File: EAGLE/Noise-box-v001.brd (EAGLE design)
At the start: 160 x 100 mm, 2 parts, among them J1 AVR_SPI_PROG_3X22X3_LOCK, U1 ATMEGA328P_TQFP

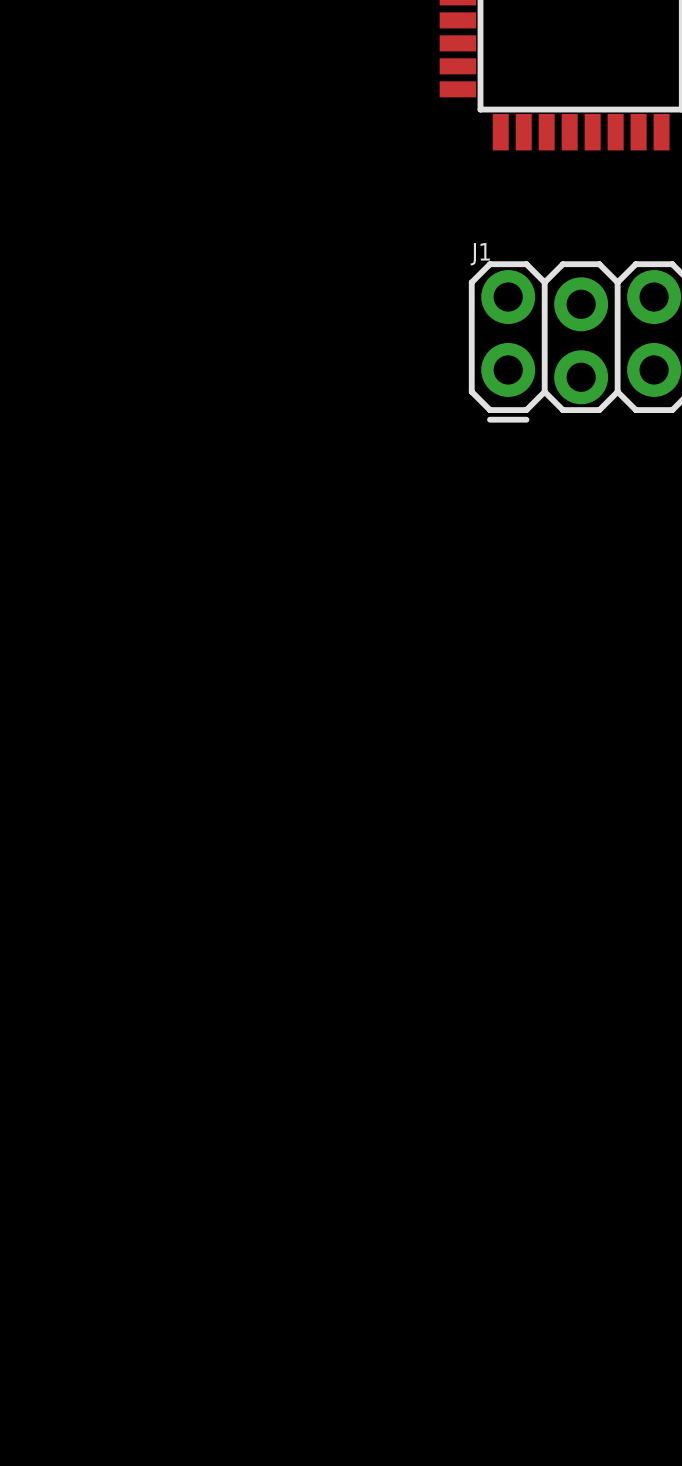
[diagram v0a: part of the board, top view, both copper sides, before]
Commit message: Sch update - power
Added voltage regulators and supporting components.
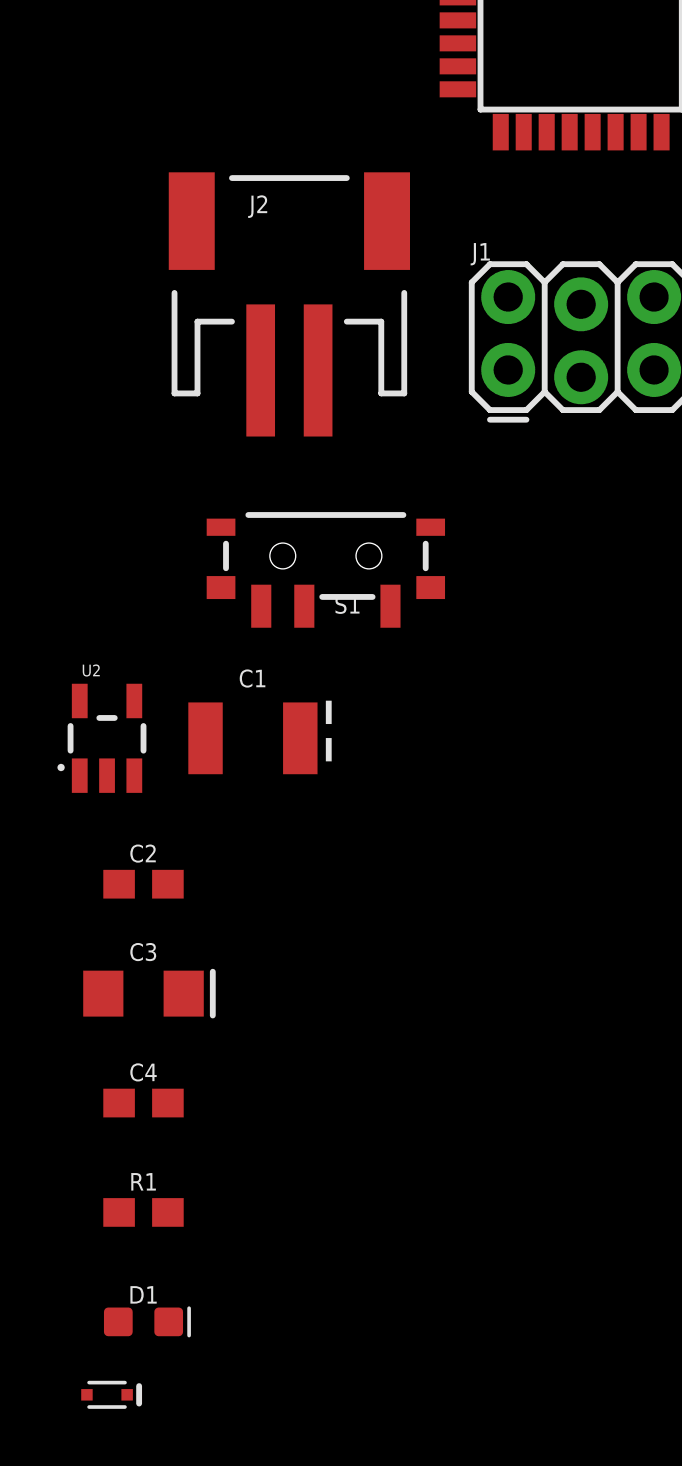
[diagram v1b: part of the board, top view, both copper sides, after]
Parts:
- added C1: 47uF, SparkFun-Capacitors:EIA3528
- added C2: 470pF, SparkFun-Capacitors:0603
- added C3: 10uF, SparkFun-Capacitors:EIA3216
- added C4: 0.1uF, SparkFun-Capacitors:0603
- added D1: RED, SparkFun-LED:LED-0603
- added D2: 120mA/40V/370mV, SparkFun-DiscreteSemi:SOD-523
- added J2: BATT, SparkFun-Connectors:JST-2-SMD
- added R1: 330, SparkFun-Resistors:0603
- added S1: (no value), SparkFun-Switches:SWITCH_SPST_SMD_A
- added U2: MIC5219 3.3V, SparkFun-IC-Power:SOT23-5
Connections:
- new net N$2: C2.1, U2.4
- new net N$3: D1.A, R1.2
- new net V+: C1.A, D2.C, S1.1, U2.1, U2.3
- new net VBATT: J2.1, S1.2
- net +3V3: now also C3.+, C4.1, D2.A, R1.1, U2.5
- net GND: now also C1.C, C2.2, C3.-, C4.2, D1.C, J2.2, U2.2
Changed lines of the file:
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@@
 </element>
 <element name="J1" library="SparkFun-Connectors" package="2X3_LOCK" value="AVR_SPI_PROG_3X22X3_LOCK" x="-7.62" y="-5.08"/>
+<element name="J2" library="SparkFun-Connectors" package="JST-2-SMD" value="BATT" x="-15.24" y="-1.27">
+<attribute name="PROD_ID" value="CONN-11443" x="-15.24" y="-1.27" size="1.778" layer="27" display="off"/>
+</element>
+<element name="S1" library="SparkFun-Switches" package="SWITCH_SPST_SMD_A" value="" x="-13.97" y="-11.43">
+<attribute name="SF_SKU" value="COM-10860" x="-13.97" y="-11.43" size="1.778" layer="27" display="off"/>
+<attribute name="PROD_ID" value="SWCH-10651" x="-13.97" y="-11.43" size="1.778" layer="27" display="off"/>
+</element>
+<element name="C1" library="SparkFun-Capacitors" package="EIA3528" value="47uF" x="-16.51" y="-17.78">
+<attribute name="PROD_ID" value="CAP-08310" x="-16.51" y="-17.78" size="1.778" layer="27" display="off"/>
+</element>
+<element name="U2" library="SparkFun-IC-Power" package="SOT23-5" value="MIC5219 3.3V" x="-21.59" y="-17.78">
+<attribute name="PROD_ID" value="VREG-09872" x="-21.59" y="-17.78" size="1.778" layer="27" display="off"/>
+</element>
+<element name="C2" library="SparkFun-Capacitors" package="0603" value="470pF" x="-20.32" y="-22.86">
+<attribute name="PROD_ID" value="CAP-07884" x="-20.32" y="-22.86" size="1.778" layer="27" display="off"/>
+</element>
+<element name="C3" library="SparkFun-Capacitors" package="EIA3216" value="10uF" x="-20.32" y="-26.67">
+<attribute name="PROD_ID" value="CAP-00811" x="-20.32" y="-26.67" size="1.778" layer="27" display="off"/>
+</element>
+<element name="C4" library="SparkFun-Capacitors" package="0603" value="0.1uF" x="-20.32" y="-30.48">
+<attribute name="PROD_ID" value="CAP-08604" x="-20.32" y="-30.48" size="1.778" layer="27" display="off"/>
+</element>
+<element name="R1" library="SparkFun-Resistors" package="0603" value="330" x="-20.32" y="-34.29">
+<attribute name="PROD_ID" value="RES-00818" x="-20.32" y="-34.29" size="1.778" layer="27" display="off"/>
+</element>
+<element name="D1" library="SparkFun-LED" package="LED-0603" value="RED" x="-20.32" y="-38.1">
+<attribute name="PROD_ID" value="DIO-00819" x="-20.32" y="-38.1" size="1.778" layer="27" display="off"/>
+</element>
+<element name="D2" library="SparkFun-DiscreteSemi" package="SOD-523" value="120mA/40V/370mV" x="-21.59" y="-40.64">
+<attribute name="PROD_ID" value="DIO-11018" x="-21.59" y="-40.64" size="1.778" layer="27" display="off"/>
+</element>
 </elements>
 <signals>
@@
 <contactref element="U1" pad="18"/>
 <contactref element="J1" pad="2"/>
+<contactref element="U2" pad="5"/>
+<contactref element="R1" pad="1"/>
+<contactref element="C3" pad="+"/>
+<contactref element="C4" pad="1"/>
+<contactref element="D2" pad="A"/>
+<wire x1="-21.17" y1="-34.29" x2="-22.29" y2="-40.64" width="0" layer="19" extent="1-1"/>
+<wire x1="-21.17" y1="-30.48" x2="-21.17" y2="-34.29" width="0" layer="19" extent="1-1"/>
+<wire x1="-18.92" y1="-26.67" x2="-21.17" y2="-30.48" width="0" layer="19" extent="1-1"/>
+<wire x1="-22.54" y1="-16.4799" x2="-18.92" y2="-26.67" width="0" layer="19" extent="1-1"/>
+<wire x1="-7.62" y1="-2.413" x2="-22.54" y2="-16.4799" width="0" layer="19" extent="1-1"/>
 <wire x1="-9.3726" y1="6.42" x2="-7.62" y2="-2.413" width="0" layer="19" extent="1-1"/>
 <wire x1="-9.3726" y1="8.02" x2="-9.3726" y2="6.42" width="0" layer="19" extent="1-1"/>
@@
 <contactref element="U1" pad="21"/>
 <contactref element="J1" pad="6"/>
+<contactref element="J2" pad="2"/>
+<contactref element="C1" pad="C"/>
+<contactref element="U2" pad="2"/>
+<contactref element="C2" pad="2"/>
+<contactref element="C3" pad="-"/>
+<contactref element="C4" pad="2"/>
+<contactref element="D1" pad="C"/>
+<wire x1="-19.47" y1="-30.48" x2="-19.443" y2="-38.1" width="0" layer="19" extent="1-1"/>
+<wire x1="-21.72" y1="-26.67" x2="-19.47" y2="-30.48" width="0" layer="19" extent="1-1"/>
+<wire x1="-19.47" y1="-22.86" x2="-21.72" y2="-26.67" width="0" layer="19" extent="1-1"/>
+<wire x1="-21.59" y1="-19.0801" x2="-19.47" y2="-22.86" width="0" layer="19" extent="1-1"/>
+<wire x1="-18.16" y1="-17.78" x2="-21.59" y2="-19.0801" width="0" layer="19" extent="1-1"/>
+<wire x1="-14.24" y1="-4.97" x2="-18.16" y2="-17.78" width="0" layer="19" extent="1-1"/>
+<wire x1="-2.54" y1="-2.413" x2="-14.24" y2="-4.97" width="0" layer="19" extent="1-1"/>
+<wire x1="-0.7874" y1="8.02" x2="-2.54" y2="-2.413" width="0" layer="19" extent="1-1"/>
 <wire x1="-9.3726" y1="7.22" x2="-0.7874" y2="8.02" width="0" layer="19" extent="1-1"/>
 <wire x1="-9.3726" y1="8.82" x2="-9.3726" y2="7.22" width="0" layer="19" extent="1-1"/>
-<wire x1="-2.54" y1="-2.413" x2="-0.7874" y2="8.02" width="0" layer="19" extent="1-1"/>
 </signal>
 <signal name="MOSI">
@@
 <contactref element="J1" pad="1"/>
 </signal>
+<signal name="VBATT">
+<contactref element="J2" pad="1"/>
+<contactref element="S1" pad="2"/>
+<wire x1="-16.24" y1="-4.97" x2="-14.72" y2="-13.18" width="0" layer="19" extent="1-1"/>
+</signal>
+<signal name="V+">
+<contactref element="C1" pad="A"/>
+<contactref element="S1" pad="1"/>
+<contactref element="U2" pad="1"/>
+<contactref element="U2" pad="3"/>
+<contactref element="D2" pad="C"/>
+<wire x1="-20.64" y1="-19.0801" x2="-20.89" y2="-40.64" width="0" layer="19" extent="1-1"/>
+<wire x1="-22.54" y1="-19.0801" x2="-20.64" y2="-19.0801" width="0" layer="19" extent="1-1"/>
+<wire x1="-14.86" y1="-17.78" x2="-20.64" y2="-19.0801" width="0" layer="19" extent="1-1"/>
+<wire x1="-16.22" y1="-13.18" x2="-14.86" y2="-17.78" width="0" layer="19" extent="1-1"/>
+</signal>
+<signal name="N$2">
+<contactref element="U2" pad="4"/>
+<contactref element="C2" pad="1"/>
+<wire x1="-20.64" y1="-16.4799" x2="-21.17" y2="-22.86" width="0" layer="19" extent="1-1"/>
+</signal>
+<signal name="N$3">
+<contactref element="R1" pad="2"/>
+<contactref element="D1" pad="A"/>
+<wire x1="-19.47" y1="-34.29" x2="-21.197" y2="-38.1" width="0" layer="19" extent="1-1"/>
+</signal>
 </signals>

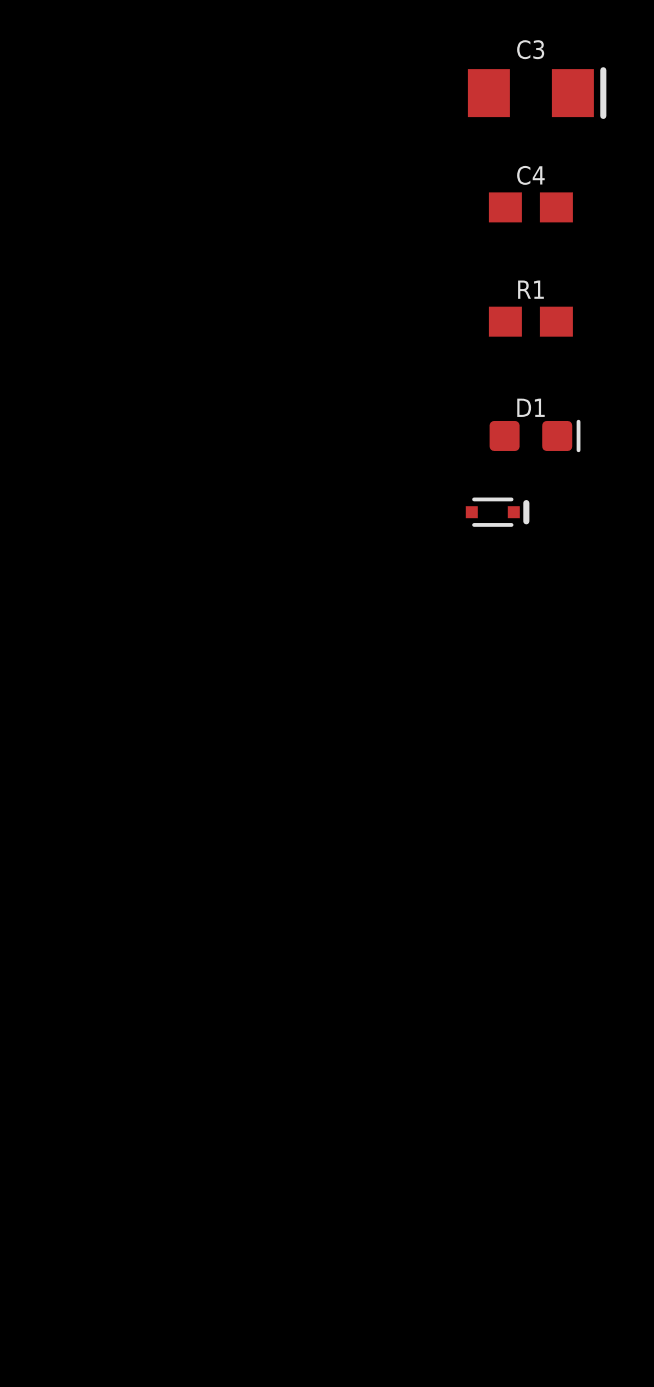
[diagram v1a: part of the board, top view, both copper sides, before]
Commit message: Schematic work
Added regulator, battery charging circuit
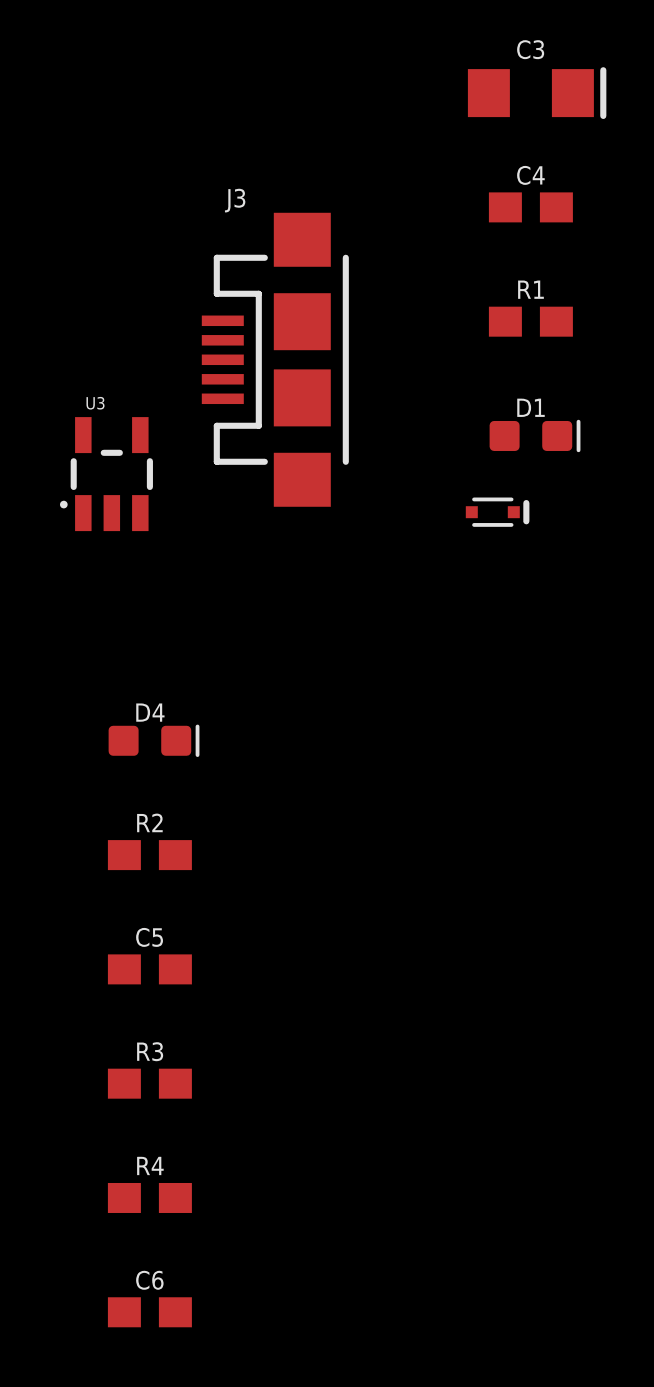
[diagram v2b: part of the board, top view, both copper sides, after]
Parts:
- added C5, C6: 4.7uF, SparkFun-Capacitors:0603
- added D4: Yellow, SparkFun-LED:LED-0603
- added J3: (no value), SparkFun-Connectors:USB-MICROB
- added R2: 330k, SparkFun-Resistors:0603
- added R3: 2.0k, SparkFun-Resistors:0603
- added R4: DNP, SparkFun-Resistors:0603
- added U3: MCP73831, SparkFun-IC-Power:SOT23-5
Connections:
- new net N$1: D4.A, R2.2
- new net N$4: R3.2, R4.2, U3.5
- new net N$5: D4.C, U3.1
- new net VIN: C5.1, J3.VBUS, R2.1, U3.4
- net GND: now also C5.2, C6.2, J3.GND, R3.1, R4.1, U3.2
- net VBATT: now also C6.1, U3.3
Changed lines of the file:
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@@
 <attribute name="PROD_ID" value="DIO-11018" x="-21.59" y="-40.64" size="1.778" layer="27" display="off"/>
+</element>
+<element name="J3" library="SparkFun-Connectors" package="USB-MICROB" value="" x="-27.94" y="-35.56">
+<attribute name="SF_ID" value="PRT-08533" x="-27.94" y="-35.56" size="1.778" layer="27" display="off"/>
+<attribute name="PROD_ID" value="CONN-09505" x="-27.94" y="-35.56" size="1.778" layer="27" display="off"/>
+</element>
+<element name="U3" library="SparkFun-IC-Power" package="SOT23-5" value="MCP73831" x="-34.29" y="-39.37">
+<attribute name="PROD_ID" value="IC-09995" x="-34.29" y="-39.37" size="1.778" layer="27" display="off"/>
+</element>
+<element name="D4" library="SparkFun-LED" package="LED-0603" value="Yellow" x="-33.02" y="-48.26">
+<attribute name="PROD_ID" value="DIO-09003" x="-33.02" y="-48.26" size="1.778" layer="27" display="off"/>
+</element>
+<element name="R2" library="SparkFun-Resistors" package="0603" value="330k" x="-33.02" y="-52.07">
+<attribute name="PROD_ID" value="RES-08968" x="-33.02" y="-52.07" size="1.778" layer="27" display="off"/>
+</element>
+<element name="C5" library="SparkFun-Capacitors" package="0603" value="4.7uF" x="-33.02" y="-55.88">
+<attribute name="PROD_ID" value="CAP-08280" x="-33.02" y="-55.88" size="1.778" layer="27" display="off"/>
+</element>
+<element name="R3" library="SparkFun-Resistors" package="0603" value="2.0k" x="-33.02" y="-59.69">
+<attribute name="PROD_ID" value="RES-08296" x="-33.02" y="-59.69" size="1.778" layer="27" display="off"/>
+</element>
+<element name="R4" library="SparkFun-Resistors" package="0603" value="DNP" x="-33.02" y="-63.5">
+<attribute name="PROD_ID" value="RES-08296" x="-33.02" y="-63.5" size="1.778" layer="27" display="off"/>
+</element>
+<element name="C6" library="SparkFun-Capacitors" package="0603" value="4.7uF" x="-33.02" y="-67.31">
+<attribute name="PROD_ID" value="CAP-08280" x="-33.02" y="-67.31" size="1.778" layer="27" display="off"/>
 </element>
 </elements>
@@
 <contactref element="C4" pad="2"/>
 <contactref element="D1" pad="C"/>
-<wire x1="-19.47" y1="-30.48" x2="-19.443" y2="-38.1" width="0" layer="19" extent="1-1"/>
-<wire x1="-21.72" y1="-26.67" x2="-19.47" y2="-30.48" width="0" layer="19" extent="1-1"/>
+<contactref element="J3" pad="GND"/>
+<contactref element="C5" pad="2"/>
+<contactref element="U3" pad="2"/>
+<contactref element="R3" pad="1"/>
+<contactref element="R4" pad="1"/>
+<contactref element="C6" pad="2"/>
+<wire x1="-33.87" y1="-59.69" x2="-33.87" y2="-63.5" width="0" layer="19" extent="1-1"/>
+<wire x1="-32.17" y1="-67.31" x2="-33.87" y2="-63.5" width="0" layer="19" extent="1-1"/>
+<wire x1="-32.17" y1="-55.88" x2="-33.87" y2="-59.69" width="0" layer="19" extent="1-1"/>
+<wire x1="-34.29" y1="-40.6701" x2="-32.17" y2="-55.88" width="0" layer="19" extent="1-1"/>
+<wire x1="-30.59" y1="-34.26" x2="-34.29" y2="-40.6701" width="0" layer="19" extent="1-1"/>
+<wire x1="-21.72" y1="-26.67" x2="-30.59" y2="-34.26" width="0" layer="19" extent="1-1"/>
+<wire x1="-19.47" y1="-30.48" x2="-21.72" y2="-26.67" width="0" layer="19" extent="1-1"/>
 <wire x1="-19.47" y1="-22.86" x2="-21.72" y2="-26.67" width="0" layer="19" extent="1-1"/>
 <wire x1="-21.59" y1="-19.0801" x2="-19.47" y2="-22.86" width="0" layer="19" extent="1-1"/>
 <wire x1="-18.16" y1="-17.78" x2="-21.59" y2="-19.0801" width="0" layer="19" extent="1-1"/>
+<wire x1="-19.443" y1="-38.1" x2="-19.47" y2="-30.48" width="0" layer="19" extent="1-1"/>
 <wire x1="-14.24" y1="-4.97" x2="-18.16" y2="-17.78" width="0" layer="19" extent="1-1"/>
 <wire x1="-2.54" y1="-2.413" x2="-14.24" y2="-4.97" width="0" layer="19" extent="1-1"/>
@@
 <contactref element="J2" pad="1"/>
 <contactref element="S1" pad="2"/>
+<contactref element="U3" pad="3"/>
+<contactref element="C6" pad="1"/>
+<wire x1="-33.34" y1="-40.6701" x2="-33.87" y2="-67.31" width="0" layer="19" extent="1-1"/>
+<wire x1="-14.72" y1="-13.18" x2="-33.34" y2="-40.6701" width="0" layer="19" extent="1-1"/>
 <wire x1="-16.24" y1="-4.97" x2="-14.72" y2="-13.18" width="0" layer="19" extent="1-1"/>
 </signal>
@@
 <wire x1="-19.47" y1="-34.29" x2="-21.197" y2="-38.1" width="0" layer="19" extent="1-1"/>
 </signal>
+<signal name="N$1">
+<contactref element="R2" pad="2"/>
+<contactref element="D4" pad="A"/>
+<wire x1="-33.897" y1="-48.26" x2="-32.17" y2="-52.07" width="0" layer="19" extent="1-1"/>
+</signal>
+<signal name="VIN">
+<contactref element="J3" pad="VBUS"/>
+<contactref element="C5" pad="1"/>
+<contactref element="R2" pad="1"/>
+<contactref element="U3" pad="4"/>
+<wire x1="-33.87" y1="-52.07" x2="-33.87" y2="-55.88" width="0" layer="19" extent="1-1"/>
+<wire x1="-33.34" y1="-38.0699" x2="-33.87" y2="-52.07" width="0" layer="19" extent="1-1"/>
+<wire x1="-30.59" y1="-36.86" x2="-33.34" y2="-38.0699" width="0" layer="19" extent="1-1"/>
+</signal>
+<signal name="N$5">
+<contactref element="D4" pad="C"/>
+<contactref element="U3" pad="1"/>
+<wire x1="-35.24" y1="-40.6701" x2="-32.143" y2="-48.26" width="0" layer="19" extent="1-1"/>
+</signal>
+<signal name="N$4">
+<contactref element="U3" pad="5"/>
+<contactref element="R3" pad="2"/>
+<contactref element="R4" pad="2"/>
+<wire x1="-32.17" y1="-59.69" x2="-32.17" y2="-63.5" width="0" layer="19" extent="1-1"/>
+<wire x1="-35.24" y1="-38.0699" x2="-32.17" y2="-59.69" width="0" layer="19" extent="1-1"/>
+</signal>
 </signals>
